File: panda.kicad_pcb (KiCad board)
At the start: 2 copper layers, 100 x 125 mm, 104 parts, among them J1 PIN6-9_Breakout, J10 Screw_Terminal_01x02, J11 24V_Lockout_Key_Switch, J12 XT60-M, J13 PT_1, J14 PT_4, J15 PT_2, J16 PT_5, J17 PT_3, J18 PT_6, J19 4-Pin Load Cell, J2 PIN10-13_Breakout, J20 5-Pin Load Cell, J21 Ignitor Screw Terminal, J3 Valve_1_PWR, J4 Valve_4_PWR, J5 Valve_2_PWR, J6 Valve_5_PWR, J7 Valve_3_PWR, J8 Valve_6_PWR, J9 Screw_Terminal_01x04, K1 G5Q-1A DC24, K2 G5Q-1A DC24, Q1 BSS138, Q2 BSS138, Q3 BSS138, Q4 BSS138, Q5 BSS138, Q6 BSS138, Q7 BSS138, Q8 BSS138, U1 ESP32-S3, U2 ADS112C04, U3 ADS112C04, U4 ADS112C04, U5 ADS112C04, U6 XC6206P332MR, U8 TPS5430DDA

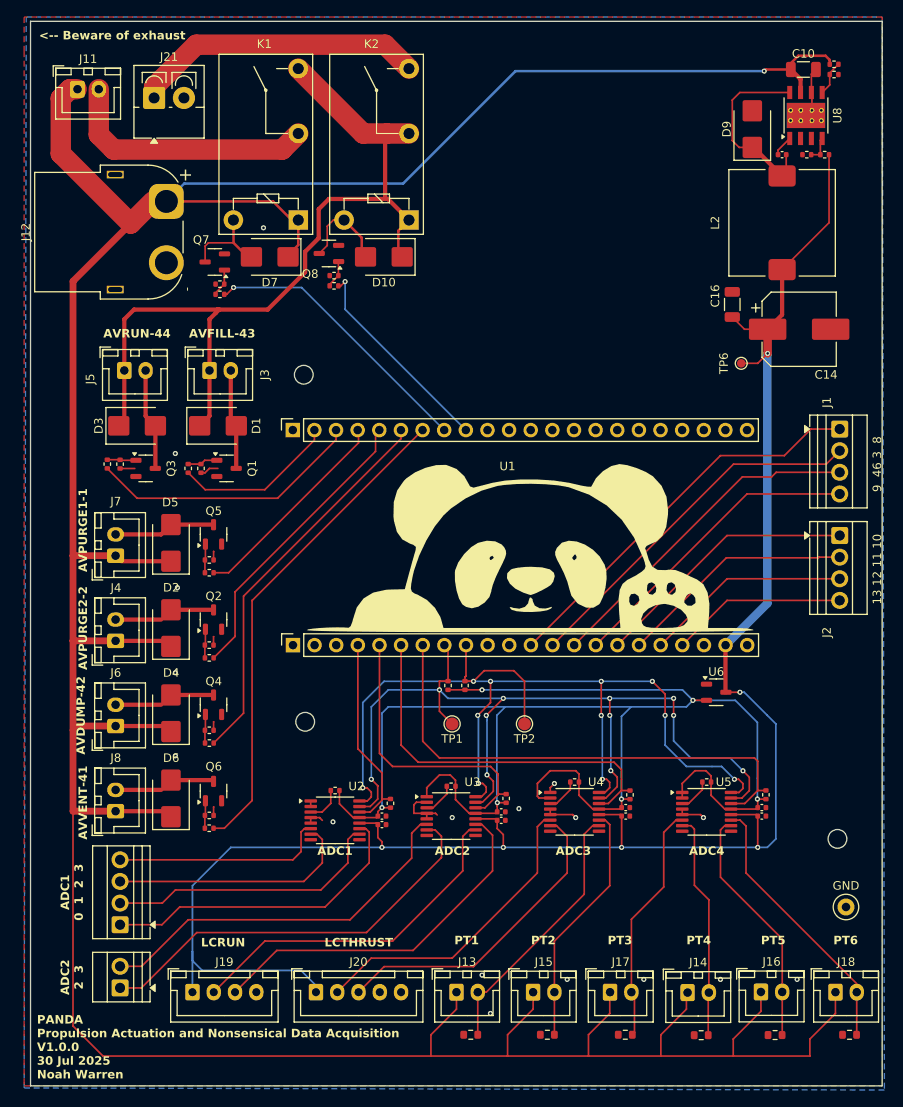
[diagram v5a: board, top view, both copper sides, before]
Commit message: Add signal conditioning. Change screw hole footprint
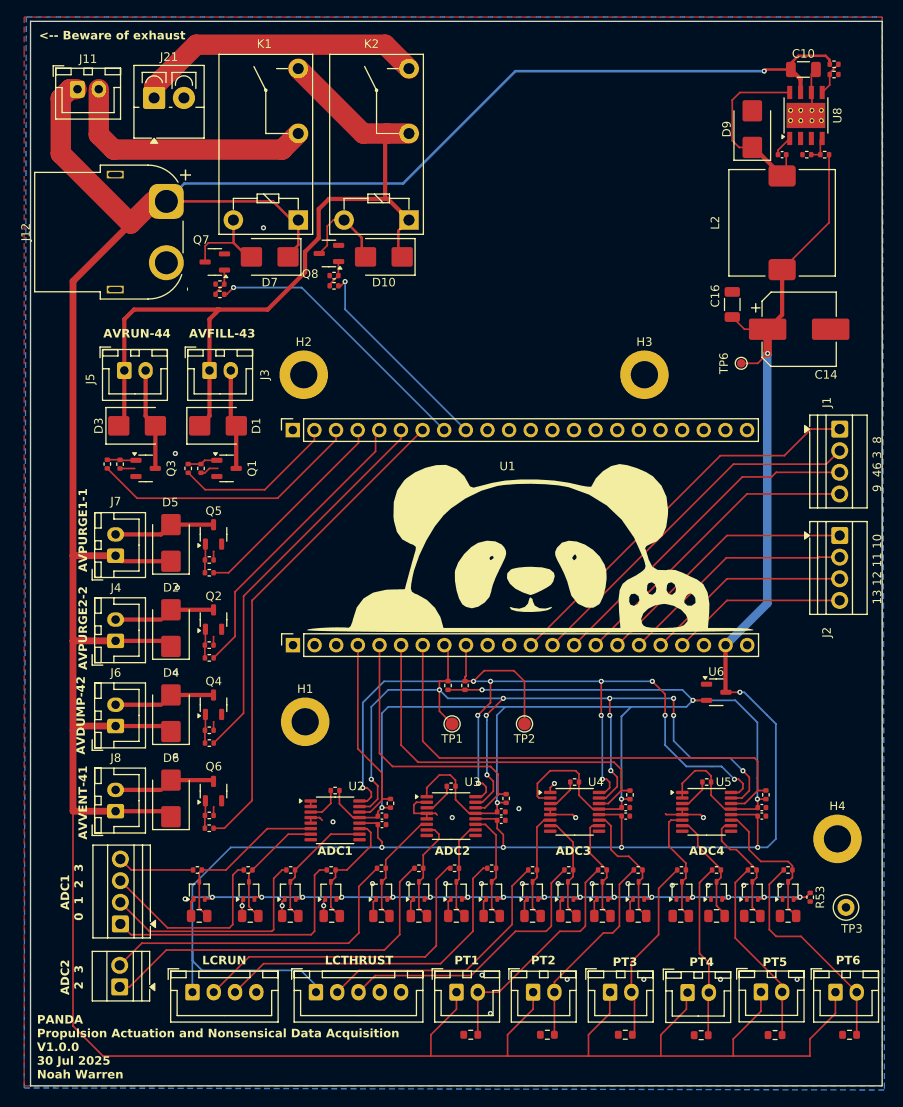
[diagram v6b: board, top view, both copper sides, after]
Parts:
- removed GND: TestPoint_Loop_D2.50mm_Drill1.0mm, TestPoint:TestPoint_Loop_D2.50mm_Drill1.0mm
- removed REF** (x3): MountingHole_2.2mm_M2, MountingHole:MountingHole_2.2mm_M2
- added C11: 68nF, Capacitor_SMD:C_0805_2012Metric, F.Cu at (136.1, 129.8)
- added C13: 68nF, Capacitor_SMD:C_0805_2012Metric, F.Cu at (145.6, 129.8)
- added C15: 68nF, Capacitor_SMD:C_0805_2012Metric, F.Cu at (140.8, 129.8)
- added C17: 68nF, Capacitor_SMD:C_0805_2012Metric, F.Cu at (151.4, 129.8)
- added C18: 68nF, Capacitor_SMD:C_0805_2012Metric, F.Cu at (164.4, 129.8)
- added C19: 68nF, Capacitor_SMD:C_0805_2012Metric, F.Cu at (155.8, 129.8)
- added C20: 68nF, Capacitor_SMD:C_0805_2012Metric, F.Cu at (160.2, 129.8)
- added C21: 68nF, Capacitor_SMD:C_0805_2012Metric, F.Cu at (169.2, 129.8)
- added C22: 68nF, Capacitor_SMD:C_0805_2012Metric, F.Cu at (181.6, 129.8)
- added C23: 68nF, Capacitor_SMD:C_0805_2012Metric, F.Cu at (173.4, 129.8)
- added C24: 68nF, Capacitor_SMD:C_0805_2012Metric, F.Cu at (177.4, 129.8)
- added C25: 68nF, Capacitor_SMD:C_0805_2012Metric, F.Cu at (186.6, 129.8)
- added C26: 68nF, Capacitor_SMD:C_0805_2012Metric, F.Cu at (199.2, 129.8)
- added C27: 68nF, Capacitor_SMD:C_0805_2012Metric, F.Cu at (190.8, 129.8)
- added C28: 68nF, Capacitor_SMD:C_0805_2012Metric, F.Cu at (195.0, 129.8)
- added C9: 68nF, Capacitor_SMD:C_0805_2012Metric, F.Cu at (130.1, 129.8)
- added D26: BAT54SW, Package_TO_SOT_SMD:SOT-323_SC-70, F.Cu at (130.1, 126.8)
- added D27: BAT54SW, Package_TO_SOT_SMD:SOT-323_SC-70, F.Cu at (135.9, 126.8)
- added D28: BAT54SW, Package_TO_SOT_SMD:SOT-323_SC-70, F.Cu at (145.5, 126.8)
- added D29: BAT54SW, Package_TO_SOT_SMD:SOT-323_SC-70, F.Cu at (140.8, 126.8)
- added D30: BAT54SW, Package_TO_SOT_SMD:SOT-323_SC-70, F.Cu at (169.2, 126.8)
- added D31: BAT54SW, Package_TO_SOT_SMD:SOT-323_SC-70, F.Cu at (181.7, 126.8)
- added D32: BAT54SW, Package_TO_SOT_SMD:SOT-323_SC-70, F.Cu at (173.3, 126.8)
- added D33: BAT54SW, Package_TO_SOT_SMD:SOT-323_SC-70, F.Cu at (177.4, 126.8)
- added D34: BAT54SW, Package_TO_SOT_SMD:SOT-323_SC-70, F.Cu at (151.5, 126.8)
- added D35: BAT54SW, Package_TO_SOT_SMD:SOT-323_SC-70, F.Cu at (164.4, 126.8)
- added D36: BAT54SW, Package_TO_SOT_SMD:SOT-323_SC-70, F.Cu at (155.8, 126.8)
- added D37: BAT54SW, Package_TO_SOT_SMD:SOT-323_SC-70, F.Cu at (160.2, 126.8)
- added D38: BAT54SW, Package_TO_SOT_SMD:SOT-323_SC-70, F.Cu at (186.7, 126.8)
- added D39: BAT54SW, Package_TO_SOT_SMD:SOT-323_SC-70, F.Cu at (199.2, 126.8)
- added D40: BAT54SW, Package_TO_SOT_SMD:SOT-323_SC-70, F.Cu at (190.8, 126.8)
- added D41: BAT54SW, Package_TO_SOT_SMD:SOT-323_SC-70, F.Cu at (195.0, 126.8)
- added H1: MountingHole_Pad, MountingHole:MountingHole_3.2mm_M3_ISO7380_Pad, F.Cu at (142.5, 107.0)
- added H2: MountingHole_Pad, MountingHole:MountingHole_3.2mm_M3_ISO7380_Pad, F.Cu at (142.3, 66.2)
- added H3: MountingHole_Pad, MountingHole:MountingHole_3.2mm_M3_ISO7380_Pad, F.Cu at (182.3, 66.2)
- added H4: MountingHole_Pad, MountingHole:MountingHole_3.2mm_M3_ISO7380_Pad, F.Cu at (205.0, 120.8)
- added R27: 2.2k, Resistor_SMD:R_0402_1005Metric, F.Cu at (129.8, 124.4)
- added R28: 2.2k, Resistor_SMD:R_0402_1005Metric, F.Cu at (135.8, 124.4)
- added R39: 2.2k, Resistor_SMD:R_0402_1005Metric, F.Cu at (140.8, 124.4)
- added R40: 2.2k, Resistor_SMD:R_0402_1005Metric, F.Cu at (145.6, 124.4)
- added R41: 2.2k, Resistor_SMD:R_0402_1005Metric, F.Cu at (151.4, 124.2)
- added R42: 2.2k, Resistor_SMD:R_0402_1005Metric, F.Cu at (155.8, 124.2)
- added R43: 2.2k, Resistor_SMD:R_0402_1005Metric, F.Cu at (160.1, 124.2)
- added R44: 2.2k, Resistor_SMD:R_0402_1005Metric, F.Cu at (164.4, 124.2)
- added R45: 2.2k, Resistor_SMD:R_0402_1005Metric, F.Cu at (169.2, 124.4)
- added R46: 2.2k, Resistor_SMD:R_0402_1005Metric, F.Cu at (173.4, 124.4)
- added R47: 2.2k, Resistor_SMD:R_0402_1005Metric, F.Cu at (177.4, 124.4)
- added R48: 2.2k, Resistor_SMD:R_0402_1005Metric, F.Cu at (181.6, 124.4)
- added R49: 2.2k, Resistor_SMD:R_0402_1005Metric, F.Cu at (186.7, 124.4)
- added R50: 2.2k, Resistor_SMD:R_0402_1005Metric, F.Cu at (190.8, 124.4)
- added R51: 2.2k, Resistor_SMD:R_0402_1005Metric, F.Cu at (195.0, 124.4)
- added R52: 2.2k, Resistor_SMD:R_0402_1005Metric, F.Cu at (199.2, 124.4)
- added R53: 10k, Resistor_SMD:R_0402_1005Metric, F.Cu at (201.8, 127.6)
- added TP3: TestPoint, TestPoint:TestPoint_Loop_D2.50mm_Drill1.0mm, F.Cu at (206.0, 128.8)
- moved J10 0.12 mm to (120.7, 138.1)
- moved J9 0.10 mm to (120.8, 130.7)
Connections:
- J10 pad 1: /ADC Circuitry/ADC2_AIN2 -> Net-(J10-Pin_1)
- J10 pad 2: /ADC Circuitry/ADC2_AIN3 -> Net-(J10-Pin_2)
- J9 pad 1: /ADC Circuitry/ADC1_AIN0 -> Net-(J9-Pin_1)
- J9 pad 2: /ADC Circuitry/ADC1_AIN1 -> Net-(J9-Pin_2)
- J9 pad 3: /ADC Circuitry/ADC1_AIN2 -> Net-(J9-Pin_3)
- J9 pad 4: /ADC Circuitry/ADC1_AIN3 -> Net-(J9-Pin_4)
- U2 pad 10: /ADC Circuitry/ADC1_AIN1 -> ADC1_AIN1
- U2 pad 11: /ADC Circuitry/ADC1_AIN0 -> ADC1_AIN0
- U2 pad 6: /ADC Circuitry/ADC1_AIN3 -> ADC1_AIN3
- U2 pad 7: /ADC Circuitry/ADC1_AIN2 -> ADC1_AIN2
- U3 pad 10: LC_FILL_+ -> ADC2_AIN1
- U3 pad 11: LC_FILL_- -> ADC2_AIN0
- U3 pad 6: /ADC Circuitry/ADC2_AIN3 -> ADC2_AIN3
- U3 pad 7: /ADC Circuitry/ADC2_AIN2 -> ADC2_AIN2
- U4 pad 10: PT_READING_1 -> ADC3_AIN1
- U4 pad 11: PT_READING_2 -> ADC3_AIN0
- U4 pad 6: LC_THRUST_+ -> ADC3_AIN3
- U4 pad 7: LC_THRUST_- -> ADC3_AIN2
- U5 pad 10: PT_READING_5 -> ADC4_AIN1
- U5 pad 11: PT_READING_6 -> ADC4_AIN0
- U5 pad 6: PT_READING_3 -> ADC4_AIN3
- U5 pad 7: PT_READING_4 -> ADC4_AIN2
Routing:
- net +5V: track 222.5 -> 308.8 mm, vias 6 -> 22
- net /ADC Circuitry/ADC2_AIN2: track 48.6 -> 0.00 mm
- net /ADC Circuitry/ADC2_AIN3: track 44.6 -> 0.00 mm
- net Net-(J10-Pin_1): track 0.00 -> 44.0 mm
- net Net-(J10-Pin_2): track 0.00 -> 38.1 mm
- net /ADC Circuitry/ADC1_AIN0: track 37.2 -> 0.00 mm
- net /ADC Circuitry/ADC1_AIN1: track 33.1 -> 0.00 mm
- net Net-(J9-Pin_1): track 0.00 -> 31.8 mm
- net /ADC Circuitry/ADC1_AIN2: track 29.0 -> 0.00 mm
- net GND: track 30.2 -> 57.6 mm, vias 18 -> 34
- net Net-(J9-Pin_2): track 0.00 -> 27.4 mm
- net /ADC Circuitry/ADC1_AIN3: track 25.3 -> 0.00 mm
- net Net-(J9-Pin_3): track 0.00 -> 23.0 mm
- net ADC1_AIN3: track 0.00 -> 20.7 mm
- net ADC4_AIN0: track 0.00 -> 17.1 mm
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
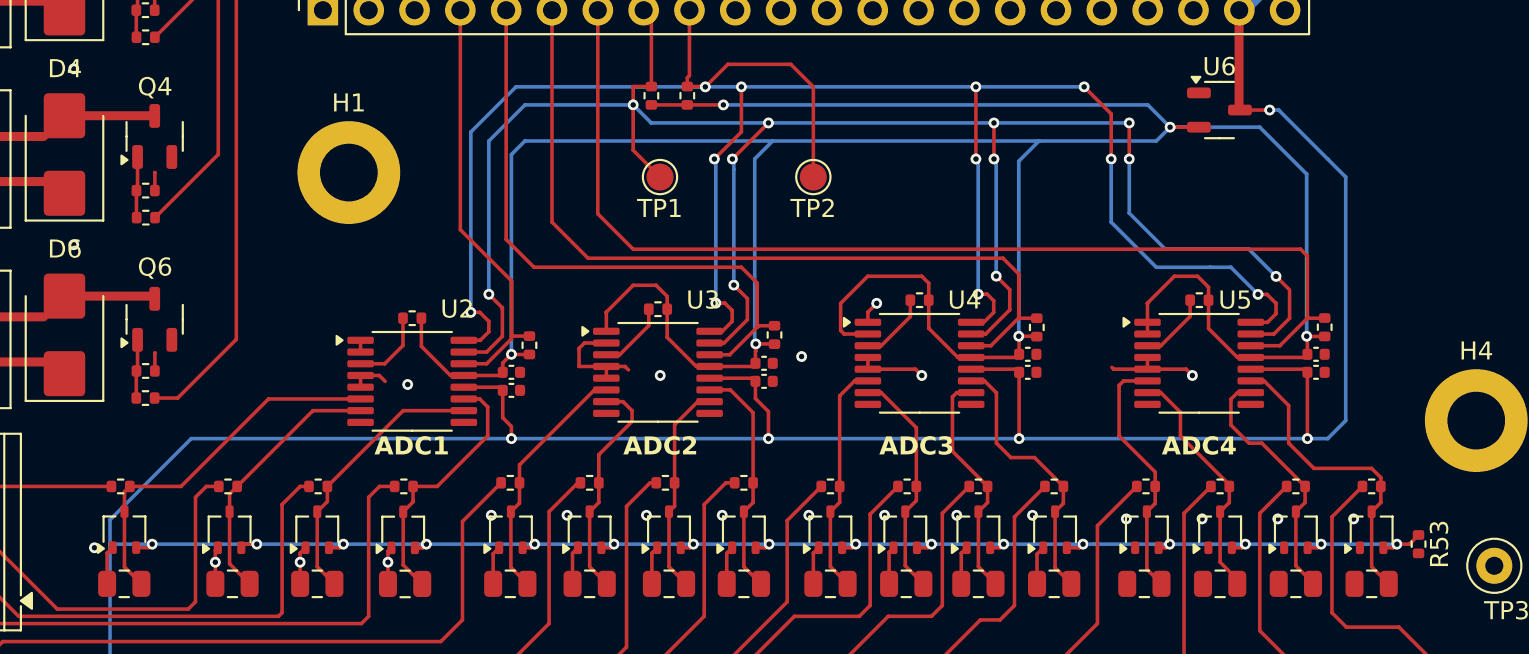
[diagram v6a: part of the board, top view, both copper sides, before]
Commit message: Update +5V rail wiring for adcs and signal conditioning
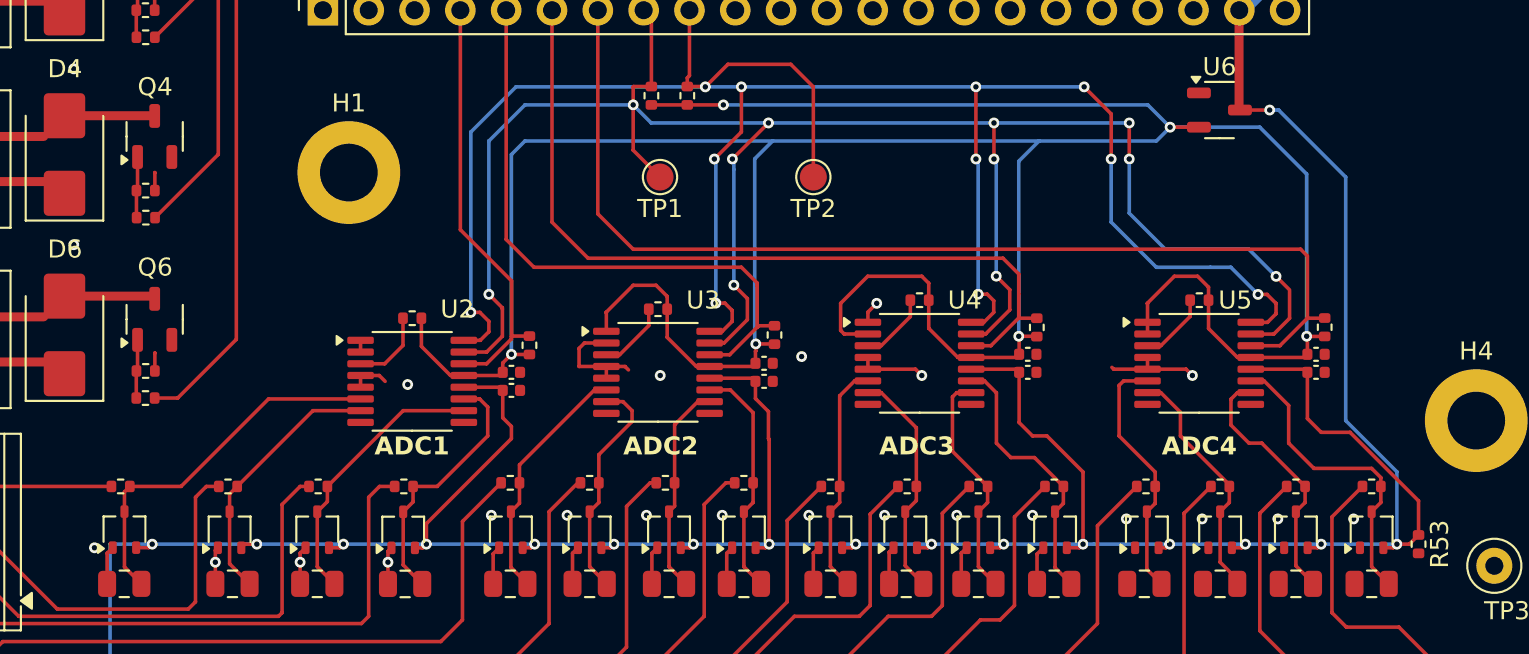
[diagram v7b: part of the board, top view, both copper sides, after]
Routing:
- net +5V: track 308.8 -> 275.2 mm, vias 22 -> 18
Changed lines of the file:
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@@
 	)
 	(segment
-		(start 195.6375 118.075)
-		(end 195.6375 121.75)
+		(start 165.8 127.6)
+		(end 165.8 121.787499)
 		(width 0.2)
 		(layer "F.Cu")
@@
 	)
 	(segment
+		(start 180.4 121.6)
+		(end 179.6575 120.8575)
+		(width 0.2)
+		(layer "F.Cu")
+		(net 3)
+	)
+	(segment
+		(start 179.6575 120.8575)
+		(end 179.6575 118.075)
+		(width 0.2)
+		(layer "F.Cu")
+		(net 3)
+	)
+	(segment
 		(start 136.74 127.6)
 		(end 136.54 127.8)
@@
 	)
 	(segment
+		(start 201.8 127.09)
+		(end 201.8 125.2)
+		(width 0.2)
+		(layer "F.Cu")
+		(net 3)
+	)
+	(segment
 		(start 131.407113 127.792887)
 		(end 131.6 127.6)
@@
 	)
 	(segment
+		(start 183.2 123.6)
+		(end 181.2 121.6)
+		(width 0.2)
+		(layer "F.Cu")
+		(net 3)
+	)
+	(segment
 		(start 146.594221 127.805779)
 		(end 146.8 127.6)
@@
 	)
 	(segment
+		(start 183.2 127.6)
+		(end 183.2 123.6)
+		(width 0.2)
+		(layer "F.Cu")
+		(net 3)
+	)
+	(segment
 		(start 164.865929 118.4)
 		(end 165.040929 118.575)
+		(width 0.2)
+		(layer "F.Cu")
+		(net 3)
+	)
+	(segment
+		(start 196.4 121.4)
+		(end 195.6375 120.6375)
 		(width 0.2)
 		(layer "F.Cu")
@@
 	)
 	(segment
+		(start 198 121.4)
+		(end 196.4 121.4)
+		(width 0.2)
+		(layer "F.Cu")
+		(net 3)
+	)
+	(segment
 		(start 162.5 118.4)
 		(end 164.865929 118.4)
@@
 	)
 	(segment
+		(start 201.8 125.2)
+		(end 198 121.4)
+		(width 0.2)
+		(layer "F.Cu")
+		(net 3)
+	)
+	(segment
 		(start 173.995 127.8)
 		(end 174.6 127.8)
+		(width 0.2)
+		(layer "F.Cu")
+		(net 3)
+	)
+	(segment
+		(start 146.8 127.6)
+		(end 146.8 126.462499)
 		(width 0.2)
 		(layer "F.Cu")
@@
 	)
 	(segment
+		(start 181.2 121.6)
+		(end 180.4 121.6)
+		(width 0.2)
+		(layer "F.Cu")
+		(net 3)
+	)
+	(segment
 		(start 165.040929 119.528428)
 		(end 165.040929 118.575)
@@
 	)
 	(segment
+		(start 146.8 126.462499)
+		(end 151.512499 121.75)
+		(width 0.2)
+		(layer "F.Cu")
+		(net 3)
+	)
+	(segment
 		(start 170.4 127.8)
 		(end 170.6 127.6)
@@
 	)
 	(segment
-		(start 179.6575 121.75)
-		(end 179.6575 118.075)
-		(width 0.2)
-		(layer "F.Cu")
-		(net 3)
-	)
-	(segment
 		(start 191.45 127.8)
 		(end 192 127.8)
@@
 	)
 	(segment
+		(start 165.8 121.787499)
+		(end 165.762501 121.75)
+		(width 0.2)
+		(layer "F.Cu")
+		(net 3)
+	)
+	(segment
 		(start 141.4 127.8)
 		(end 142 127.8)
@@
 	)
 	(segment
+		(start 195.6375 120.6375)
+		(end 195.6375 118.075)
+		(width 0.2)
+		(layer "F.Cu")
+		(net 3)
+	)
+	(segment
 		(start 179.4825 117.9)
 		(end 179.6575 118.075)
@@
 	)
 	(via
-		(at 179.6575 121.75)
-		(size 0.6)
-		(drill 0.3)
-		(layers "F.Cu" "B.Cu")
-		(net 3)
-	)
-	(via
 		(at 161.6 127.6)
 		(size 0.6)
@@
 	)
 	(via
-		(at 151.512499 121.75)
-		(size 0.6)
-		(drill 0.3)
-		(layers "F.Cu" "B.Cu")
-		(net 3)
-	)
-	(via
 		(at 183.2 127.6)
 		(size 0.6)
@@
 	)
 	(via
-		(at 195.6375 121.75)
-		(size 0.6)
-		(drill 0.3)
-		(layers "F.Cu" "B.Cu")
-		(net 3)
-	)
-	(via
 		(at 192.2 127.6)
 		(size 0.6)
@@
 	(via
 		(at 193.547184 103.534683)
-		(size 0.6)
-		(drill 0.3)
-		(layers "F.Cu" "B.Cu")
-		(net 3)
-	)
-	(via
-		(at 165.762501 121.75)
 		(size 0.6)
 		(drill 0.3)
@@
 	)
 	(segment
-		(start 133.762501 121.75)
-		(end 129.262501 126.25)
-		(width 0.2)
-		(layer "B.Cu")
-		(net 3)
-	)
-	(segment
-		(start 129.262501 126.25)
-		(end 129.262501 127.6)
-		(width 0.2)
-		(layer "B.Cu")
-		(net 3)
-	)
-	(segment
 		(start 200.6 127.6)
 		(end 200.8 127.6)
@@
 	)
 	(segment
-		(start 196.762501 106.25)
-		(end 197.762501 107.25)
-		(width 0.2)
-		(layer "B.Cu")
-		(net 3)
-	)
-	(segment
-		(start 195.6375 121.75)
-		(end 179.762501 121.75)
-		(width 0.2)
-		(layer "B.Cu")
-		(net 3)
-	)
-	(segment
 		(start 182.8 127.6)
 		(end 183.2 127.6)
@@
 	)
 	(segment
+		(start 200.6 127.6)
+		(end 200.6 123.587499)
+		(width 0.2)
+		(layer "B.Cu")
+		(net 3)
+	)
+	(segment
 		(start 142 136.2)
 		(end 130.4 136.2)
@@
 	)
 	(segment
-		(start 179.6575 121.75)
-		(end 165.762501 121.75)
-		(width 0.2)
-		(layer "B.Cu")
-		(net 3)
-	)
-	(segment
 		(start 174.8 127.6)
 		(end 178.8 127.6)
@@
 	)
 	(segment
-		(start 193.547184 103.534683)
+		(start 197.762501 107.25)
 		(end 194.047184 103.534683)
+		(width 0.2)
+		(layer "B.Cu")
+		(net 3)
+	)
+	(segment
+		(start 194.047184 103.534683)
+		(end 193.547184 103.534683)
 		(width 0.2)
 		(layer "B.Cu")
@@
 		(start 137.4 127.6)
 		(end 142.2 127.6)
-		(width 0.2)
-		(layer "B.Cu")
-		(net 3)
-	)
-	(segment
-		(start 194.047184 103.534683)
-		(end 196.762501 106.25)
 		(width 0.2)
 		(layer "B.Cu")
@@
 	)
 	(segment
+		(start 200.6 123.587499)
+		(end 197.762501 120.75)
+		(width 0.2)
+		(layer "B.Cu")
+		(net 3)
+	)
+	(segment
 		(start 143.762501 138.75)
 		(end 143.762501 137.962501)
@@
 	)
 	(segment
+		(start 197.762501 120.75)
+		(end 197.762501 107.25)
+		(width 0.2)
+		(layer "B.Cu")
+		(net 3)
+	)
+	(segment
 		(start 129.262501 127.6)
 		(end 129.262501 134)
-		(width 0.2)
-		(layer "B.Cu")
-		(net 3)
-	)
-	(segment
-		(start 151.512499 121.75)
-		(end 133.762501 121.75)
 		(width 0.2)
 		(layer "B.Cu")
@@
 	)
 	(segment
-		(start 197.762501 107.25)
-		(end 197.762501 120.75)
-		(width 0.2)
-		(layer "B.Cu")
-		(net 3)
-	)
-	(segment
-		(start 165.762501 121.75)
-		(end 151.762501 121.75)
-		(width 0.2)
-		(layer "B.Cu")
-		(net 3)
-	)
-	(segment
-		(start 196.762501 121.75)
-		(end 197.762501 120.75)
-		(width 0.2)
-		(layer "B.Cu")
-		(net 3)
-	)
-	(segment
 		(start 196.4 127.6)
 		(end 200.6 127.6)
 		(width 0.2)
 		(layer "B.Cu")
-		(net 3)
-	)
-	(segment
-		(start 179.762501 121.75)
-		(end 179.6575 121.75)
-		(width 0.2)
-		(layer "B.Cu")
-		(net 3)
-	)
-	(segment
-		(start 195.6375 121.75)
-		(end 196.762501 121.75)
-		(width 0.2)
-		(layer "B.Cu")
